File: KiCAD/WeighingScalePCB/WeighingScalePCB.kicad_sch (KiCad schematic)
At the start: 60 parts, among them IC1 MAX6675ISA+T, IC2 APS11753KMDALX-9PL5, J1 Conn_01x04_Pin, J2 AudioJack4, J3 Conn_01x14_Pin, J4 Battery Conn, J5 buzzer conn, Q2 NX138AKR, Q3 NX138AKR, Q4 NX138AKR, Q5 NX138AKR, T1 TouchPad, T2 TouchPad, U1 XIAO-ESP32-S3-SMD, U10 LMC555xMM, U2 HX711, U3 LMC555xMM, U4 74LVC1G79GW-Q100H, U5 TTP223-BA6, U6 TTP223-BA6, U7 74LVC1G79GW-Q100H, U8 74LVC1G04, U9 74LVC1G08

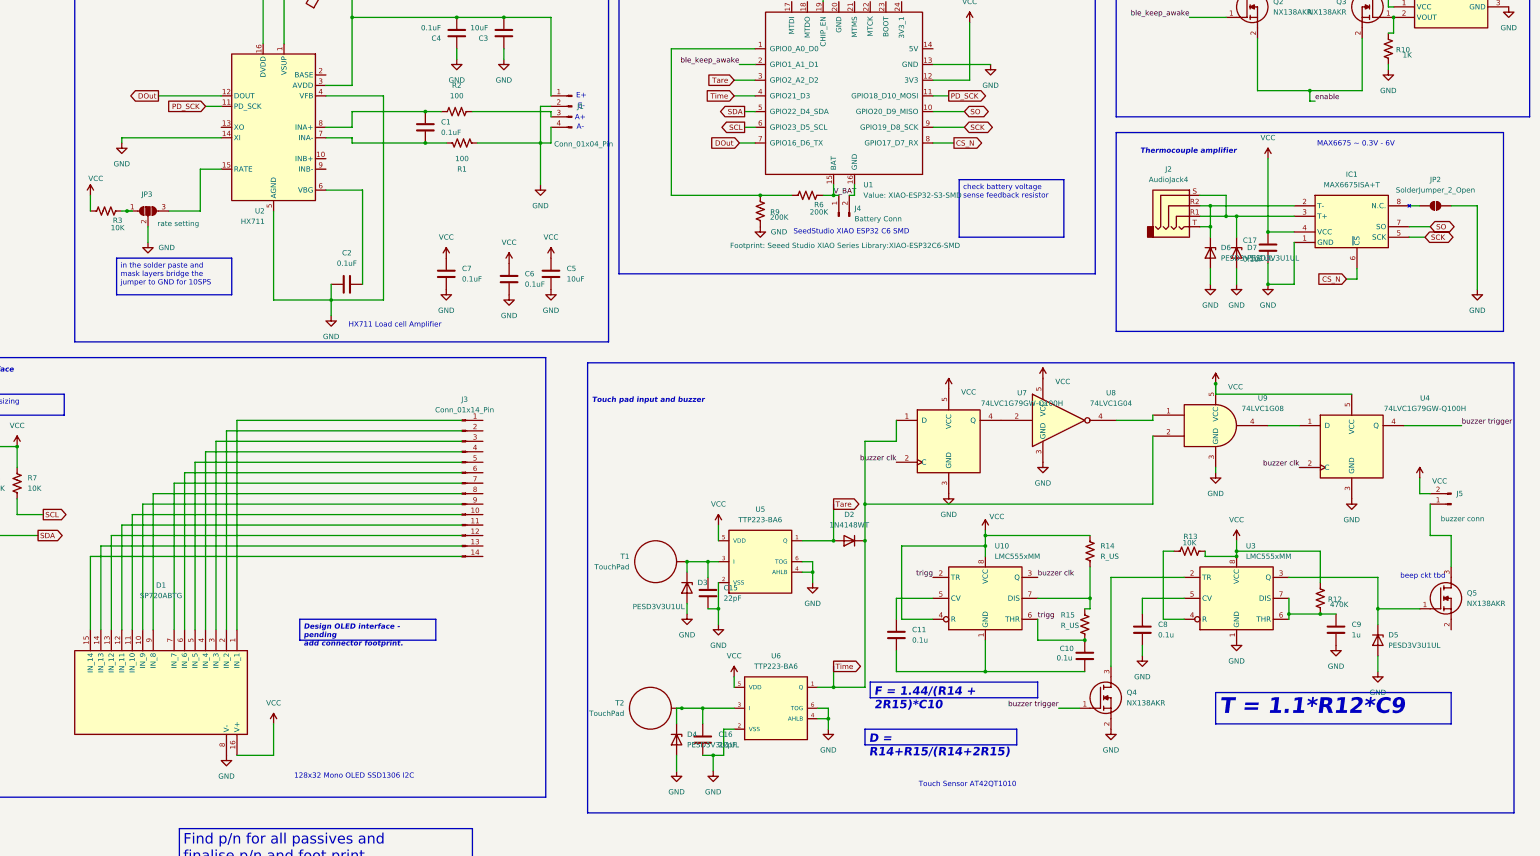
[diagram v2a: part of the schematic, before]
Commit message: assigned footprints
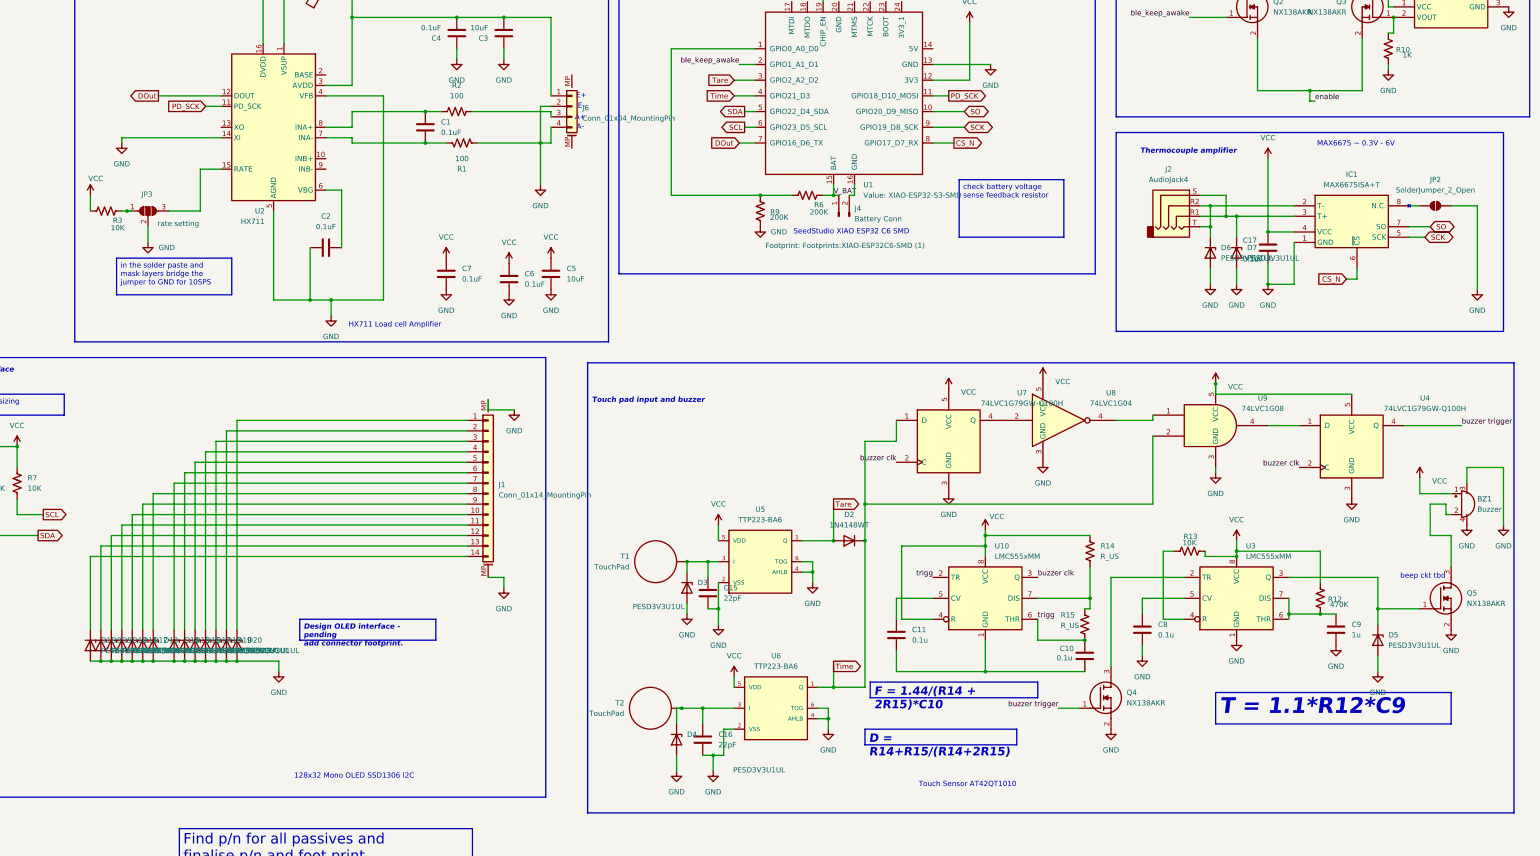
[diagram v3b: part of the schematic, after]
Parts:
- removed D1: SP720ABTG, SOIC127P600X175-16N, symbol ESD diode:SP720ABTG
- removed J1: Conn_01x04_Pin, Connector_PinHeader_1.00mm:PinHeader_1x04_P1.00mm_Vertical, symbol Connector:Conn_01x04_Pin
- removed J3: Conn_01x14_Pin, symbol Connector:Conn_01x14_Pin
- removed J5: buzzer conn, symbol Connector:Conn_01x02_Pin
- added BZ1: Buzzer, Footprints:CL7525A_buzzer, symbol Device:Buzzer
- added D1, D10, D11, D12, D13, D14, D15, D16, D17, D18, D19, D20, D8, D9: PESD3V3U1UL, Diode_SMD:D_SOD-882, symbol Diode:PESD3V3U1UL
- added J1: Conn_01x14_MountingPin, Footprints:SFV14R3STBE1HLF_oled_conn, symbol Connector_Generic_MountingPin:Conn_01x14_MountingPin
- added J6: Conn_01x04_MountingPin, Footprints:SM04B-SRSS-TB_LFSN_, symbol Connector_Generic_MountingPin:Conn_01x04_MountingPin
- IC1: footprint SOIC127P600X175-8N -> Footprints:SOIC127P600X175-8N_MAX6675
- J2: footprint (none) -> Footprints:PRT12639_thermocouple_conn
- J4: footprint (none) -> Connector_PinHeader_2.00mm:PinHeader_2x01_P2.00mm_Vertical_SMD
- Q2, Q3, Q4, Q5: footprint SOT95P230X110-3N -> Footprints:SOT95P230X110-3N
- T1, T2: footprint 0my_project:Touch-Pad_10mm -> Footprints:touchpad
- U1: footprint Seeed Studio XIAO Series Library:XIAO-ESP32C6-SMD -> Footprints:XIAO-ESP32C6-SMD (1)
- U5, U6: footprint TTP223-BA6:SOT23-6 -> Footprints:SOT23-6_touchpad_sensor
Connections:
- net GND: now also Q5.2 (S), BZ1.3 (+), BZ1.4 (+), D1.2 (A), D10.2 (A), D11.2 (A), D12.2 (A), D13.2 (A), D14.2 (A), D15.2 (A), D16.2 (A), D17.2 (A), D18.2 (A), D19.2 (A), D20.2 (A), D8.2 (A), D9.2 (A), J1.MP (MountPin), J6.2 (Pin_2), J6.4 (Pin_4)
- net VCC: now also BZ1.1 (+)
- net at C3.2, C4.2, FB1.2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: now also J6.1 (Pin_1)
- net at R2.1: now also J6.3 (Pin_3)
- net at Q5.3 (D): now also BZ1.2 (-)
- new net: D16.1 (K), J1.5 (Pin_5)
- new net: D11.1 (K), J1.10 (Pin_10)
- new net: D8.1 (K), J1.13 (Pin_13)
- new net: D20.1 (K), J1.1 (Pin_1)
- new net: D10.1 (K), J1.11 (Pin_11)
- new net: D9.1 (K), J1.12 (Pin_12)
- new net: D1.1 (K), J1.14 (Pin_14)
- new net: D19.1 (K), J1.2 (Pin_2)
- new net: D18.1 (K), J1.3 (Pin_3)
- new net: D17.1 (K), J1.4 (Pin_4)
- new net: D15.1 (K), J1.6 (Pin_6)
- new net: D14.1 (K), J1.7 (Pin_7)
- new net: D13.1 (K), J1.8 (Pin_8)
- new net: D12.1 (K), J1.9 (Pin_9)
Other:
- moved on the sheet: C2

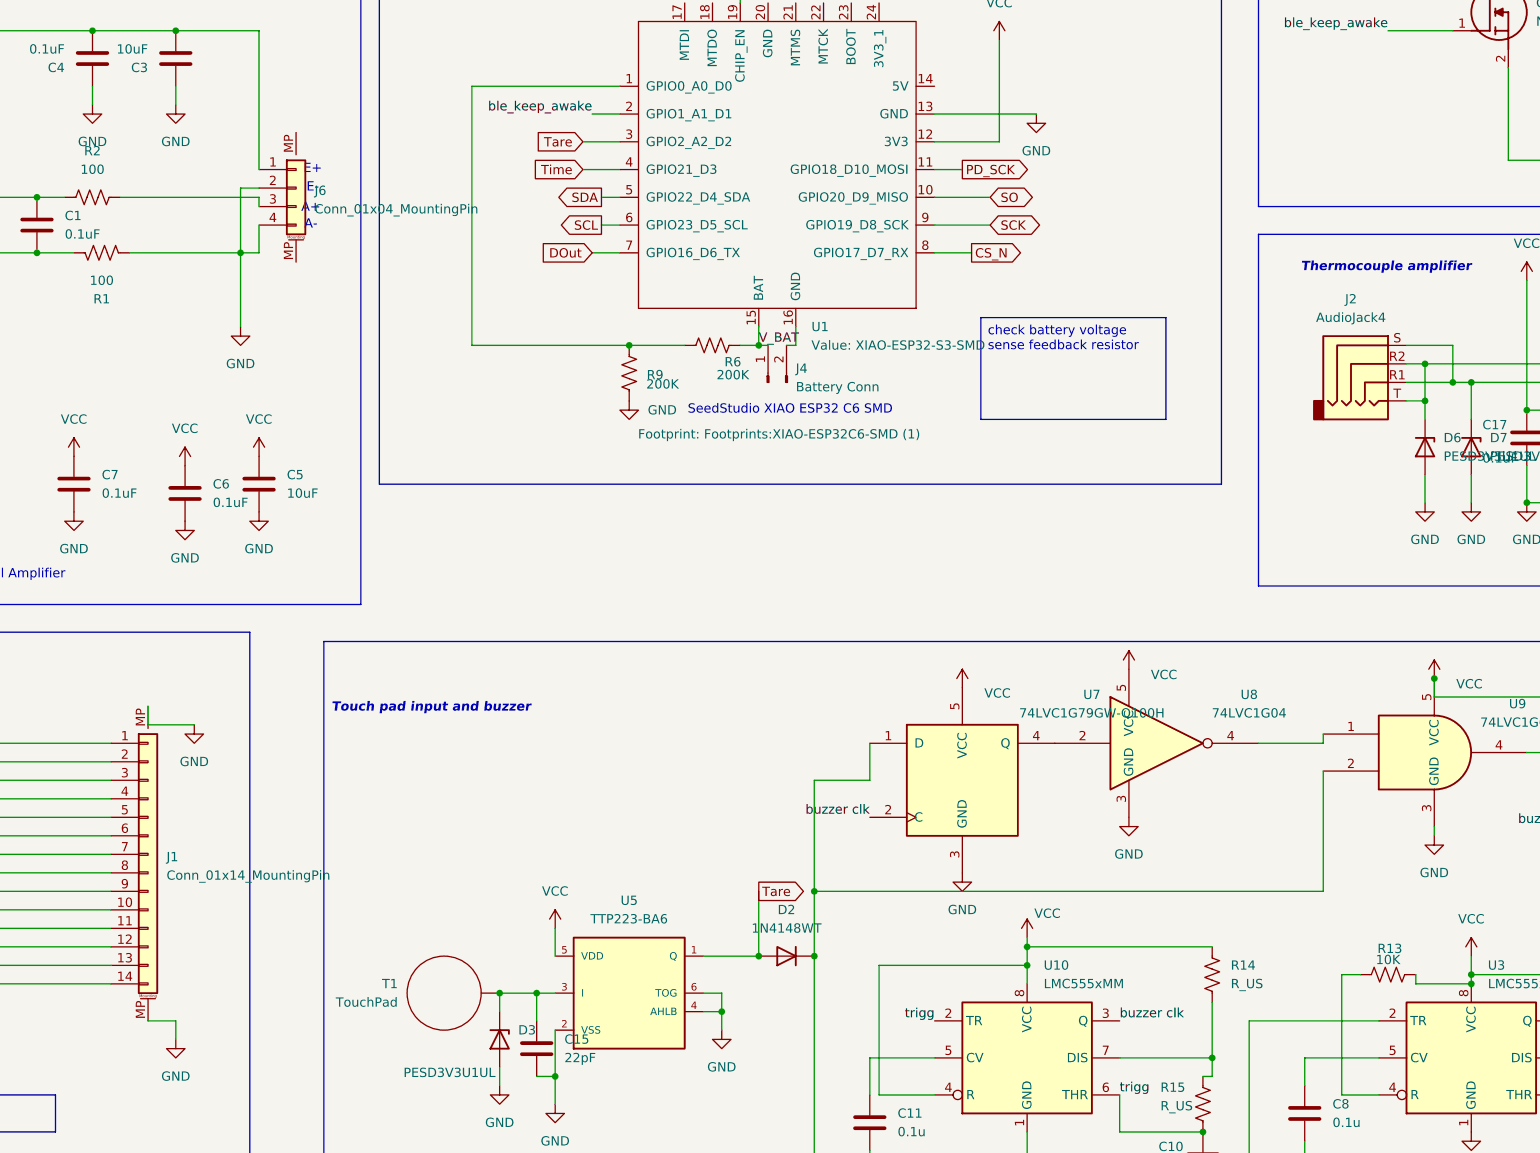
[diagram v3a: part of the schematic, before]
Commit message: added toucpad and all fps, only ferrite selection pending
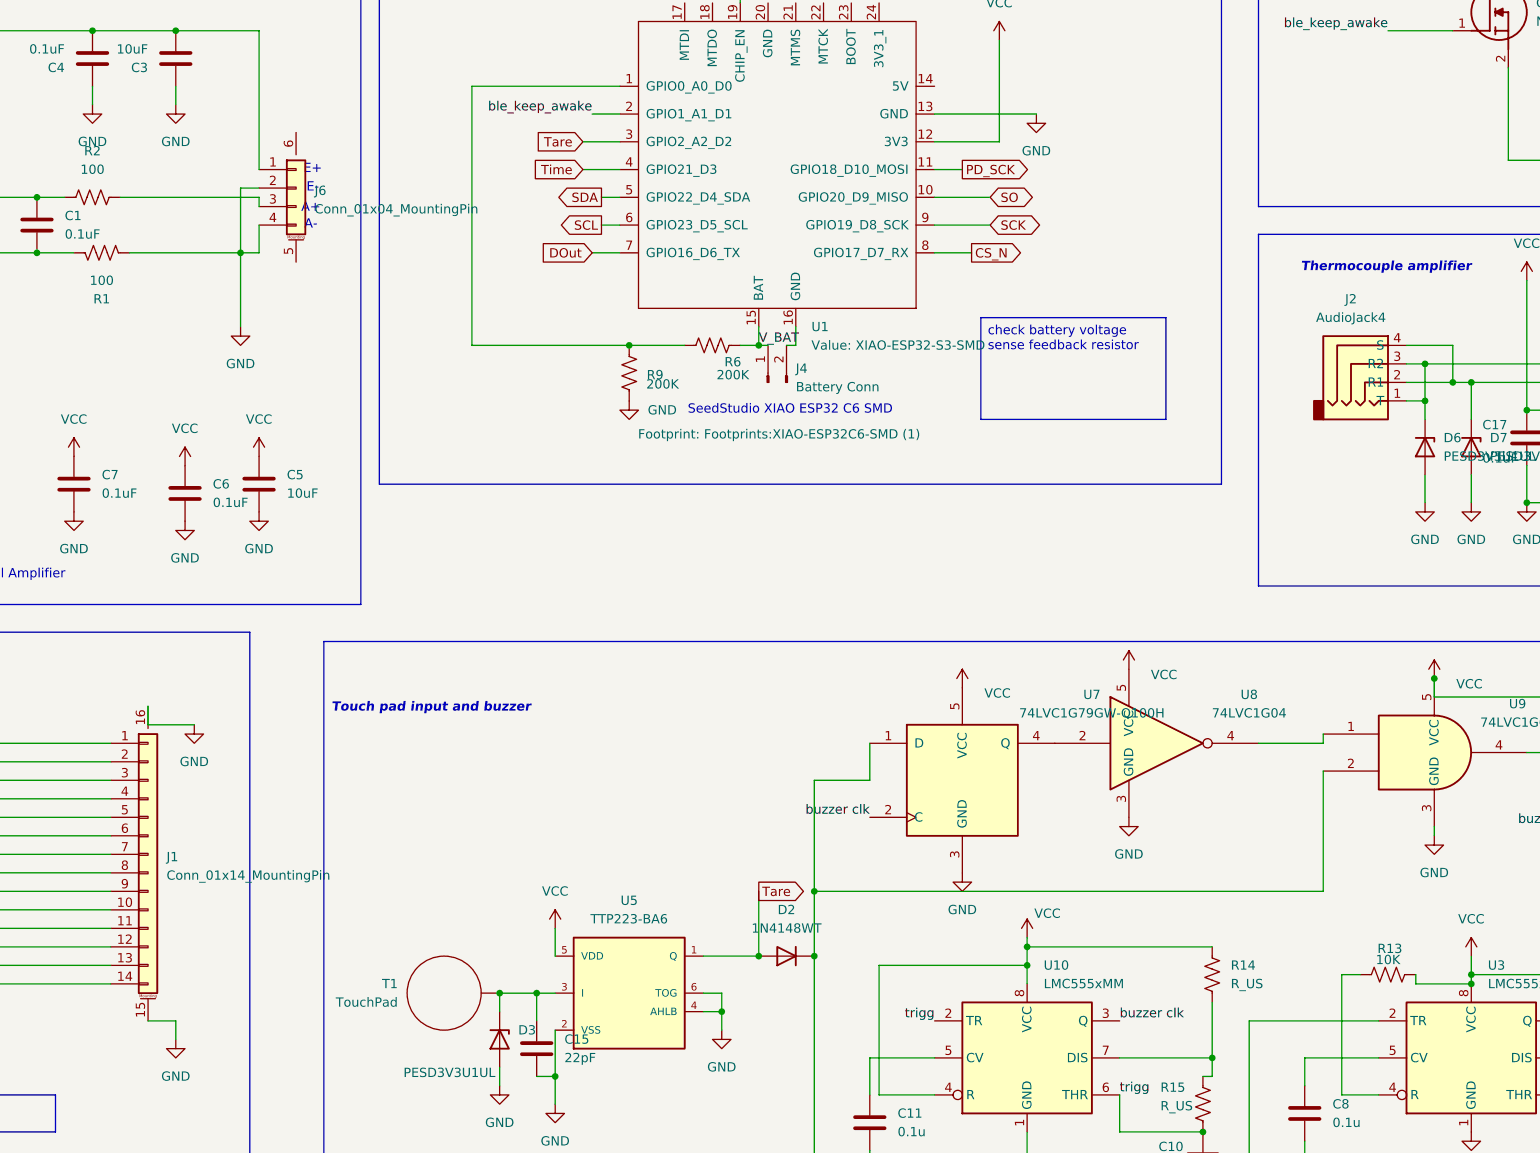
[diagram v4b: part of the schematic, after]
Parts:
- IC2: footprint SOT95P240X115-3N -> Footprints:SOT95P240X115-3N_Hall effect
- JP2: footprint (none) -> Jumper:SolderJumper-2_P1.3mm_Open_RoundedPad1.0x1.5mm
- JP3: footprint (none) -> Jumper:SolderJumper-3_P1.3mm_Open_RoundedPad1.0x1.5mm
- T2: footprint Footprints:touchpad -> Footprints:touchpad 2
- U4, U7: footprint (none) -> Footprints:SOT65P212X110-5N_D_FF
- U8: footprint (none) -> Footprints:SOT65P210X110-5N_NOT
- U9: footprint (none) -> Footprints:SOT65P212X110-5N_AND
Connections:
- net GND: now also J1.15 (MountPin), J1.16 (MountPin); no longer J1.MP (MountPin)
- net at D6.1 (K), IC1.2 (T-): now also J2.1 (T), J2.3 (R2); no longer J2.R2, J2.T
- net at D7.1 (K), IC1.3 (T+): now also J2.2 (R1), J2.4 (S); no longer J2.R1, J2.S
- net at C16.1, D4.1 (K), U6.3 (I): now also T2.T2 (Pad); no longer T2.1 (Pad)
- net at C15.1, D3.1 (K), U5.3 (I): now also T1.T1 (Pad); no longer T1.1 (Pad)
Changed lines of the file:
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@@
 			)
 		)
-		(pin "1"
+		(pin "T1"
 		)
 		(instances
@@
 		(pin "2"
 		)
-		(pin "MP"
+		(pin "6"
 		)
-		(pin "MP"
+		(pin "5"
 		)
 		(instances
@@
 			)
 		)
-		(property "Footprint" ""
+		(property "Footprint" "Footprints:SOT65P212X110-5N_D_FF"
 			(at 361.95 148.59 0)
 			(effects
@@
 		(pin "5"
 		)
-		(pin "MP"
+		(pin "16"
 		)
 		(pin "3"
@@
 		(pin "2"
 		)
-		(pin "MP"
+		(pin "15"
 		)
 		(instances
@@
 			)
 		)
-		(property "Footprint" ""
+		(property "Footprint" "Footprints:SOT65P212X110-5N_D_FF"
 			(at 264.16 147.32 0)
 			(effects
@@
 			)
 		)
-		(pin "R1"
+		(pin "2"
 		)
-		(pin "R2"
+		(pin "1"
 		)
-		(pin "S"
+		(pin "4"
 		)
-		(pin "T"
+		(pin "3"
 		)
 		(instances
@@
 			)
 		)
-		(property "Footprint" ""
+		(property "Footprint" "Jumper:SolderJumper-2_P1.3mm_Open_RoundedPad1.0x1.5mm"
 			(at 382.27 90.17 0)
 			(effects
@@
 			)
 		)
-		(property "Footprint" ""
+		(property "Footprint" "Footprints:SOT65P212X110-5N_AND"
 			(at 328.93 143.51 0)
 			(effects
@@
 			)
 		)
-		(property "Footprint" ""
+		(property "Footprint" "Footprints:SOT65P210X110-5N_NOT"
 			(at 292.1 142.24 0)
 			(effects
@@
 			)
 		)
-		(property "Footprint" ""
+		(property "Footprint" "Jumper:SolderJumper-3_P1.3mm_Open_RoundedPad1.0x1.5mm"
 			(at 69.85 91.44 0)
 			(effects
@@
 	)
 	(symbol
+		(lib_name "TouchPad_1")
 		(lib_id "0my_project:TouchPad")
 		(at 191.77 212.09 0)
@@
 			)
 		)
-		(property "Footprint" "Footprints:touchpad"
+		(property "Footprint" "Footprints:touchpad 2"
 			(at 191.77 212.09 0)
 			(effects
@@
 			)
 		)
-		(pin "1"
+		(pin "T2"
 		)
 		(instances
@@
 			)
 		)
-		(property "Footprint" "SOT95P240X115-3N"
+		(property "Footprint" "Footprints:SOT95P240X115-3N_Hall effect"
 			(at 396.24 136.83 0)
 			(effects

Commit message: added gnd plane fixed touch pad footprint, desiganed thermocouple amp, added ttp base ckt
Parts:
- removed D1, D14, D15, D8, D9: PESD3V3U1UL, Diode_SMD:D_SOD-882, symbol Diode:PESD3V3U1UL
- removed JP2: SolderJumper_2_Open, Jumper:SolderJumper-2_P1.3mm_Open_RoundedPad1.0x1.5mm, symbol Jumper:SolderJumper_2_Open
- added C12, C13, C14, C18: 1uF, Capacitor_SMD:C_0603_1608Metric, symbol Device:C
- added D15, D9: 1N4148WT, Diode_SMD:D_SOD-523, symbol Diode:1N4148WT
- added R4: 10K, Resistor_SMD:R_0402_1005Metric, symbol Device:R_US
- added R5: 330K, Resistor_SMD:R_0402_1005Metric, symbol Device:R_US
- R10: now not fitted
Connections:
- net GND: now also J1.13 (Pin_13), J1.14 (Pin_14), J1.7 (Pin_7), J4.2 (Pin_2), U1.16 (GND), C14.1, C18.1, R5.1
- net SCL: now also D11.1 (K), J1.10 (Pin_10)
- net SDA: now also D10.1 (K), J1.11 (Pin_11)
- net Time: now also D9.2 (A); no longer D2.1 (K), U7.1 (D), U9.2
- net VCC: now also D13.1 (K), D16.1 (K), J1.5 (Pin_5), J1.8 (Pin_8), C14.2, C18.2, R4.1
- net T+: now reaches D6.1 (K), IC1.2 (T-), J2.1 (T), J2.3 (R2)
- net T-: now reaches D7.1 (K), IC1.3 (T+), J2.2 (R1), J2.4 (S)
- net touch2: now reaches C16.1, D4.1 (K), T2.T2 (Pad), U6.3 (I)
- net touch1: now reaches C15.1, D3.1 (K), T1.T1 (Pad), U5.3 (I)
- net DVDD_ldcell: now reaches C3.2, C4.2, FB1.2, J6.1 (Pin_1), U2.3 (AVDD)
- net c12_1: now reaches D20.1 (K), J1.1 (Pin_1)
- net c12_1: now also C12.2
- net R5: now reaches J1.12 (Pin_12)
- net R5: now also R5.2
- net c12_2: now reaches D19.1 (K), J1.2 (Pin_2)
- net c12_2: now also C12.1
- net c13_1: now reaches D18.1 (K), J1.3 (Pin_3)
- net c13_1: now also C13.2
- net c13_2: now reaches D17.1 (K), J1.4 (Pin_4)
- net c13_2: now also C13.1
- net d15: now reaches D12.1 (K), J1.9 (Pin_9)
- net d15: now also D15.1 (K)
- new net: D15.2 (A), R4.2
- new net timeORtare: D2.1 (K), D9.1 (K), U7.1 (D), U9.2
- no-connect marks 0 -> 13
